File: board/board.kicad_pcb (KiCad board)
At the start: 2 copper layers, 21 x 61 mm, 16 parts, among them J1 002_SPI_2x5, J3 007_ADC_2x5, J4 007_ADC_2x5, J5 007_ADC_2x5, J6 007_ADC_2x5, U1 ADS131M08, Y1 8MhZ

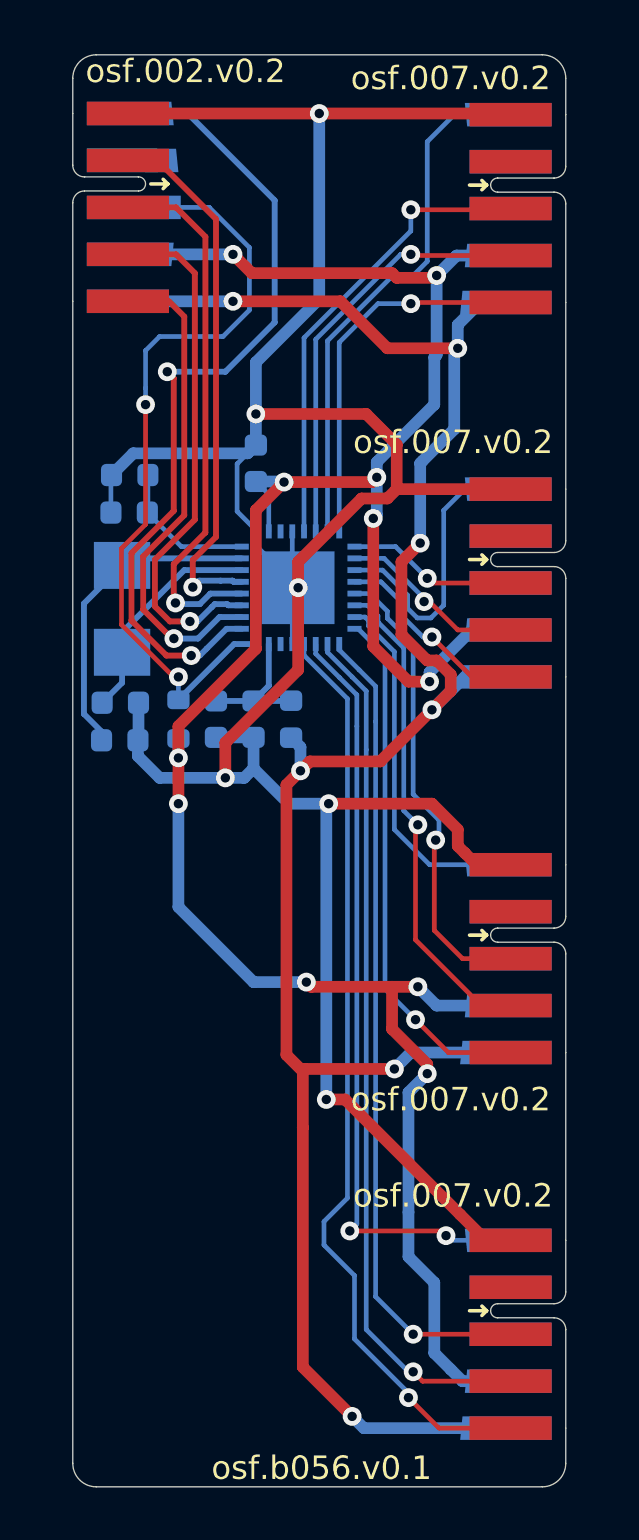
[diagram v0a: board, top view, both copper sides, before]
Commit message: separated gnd and agnd
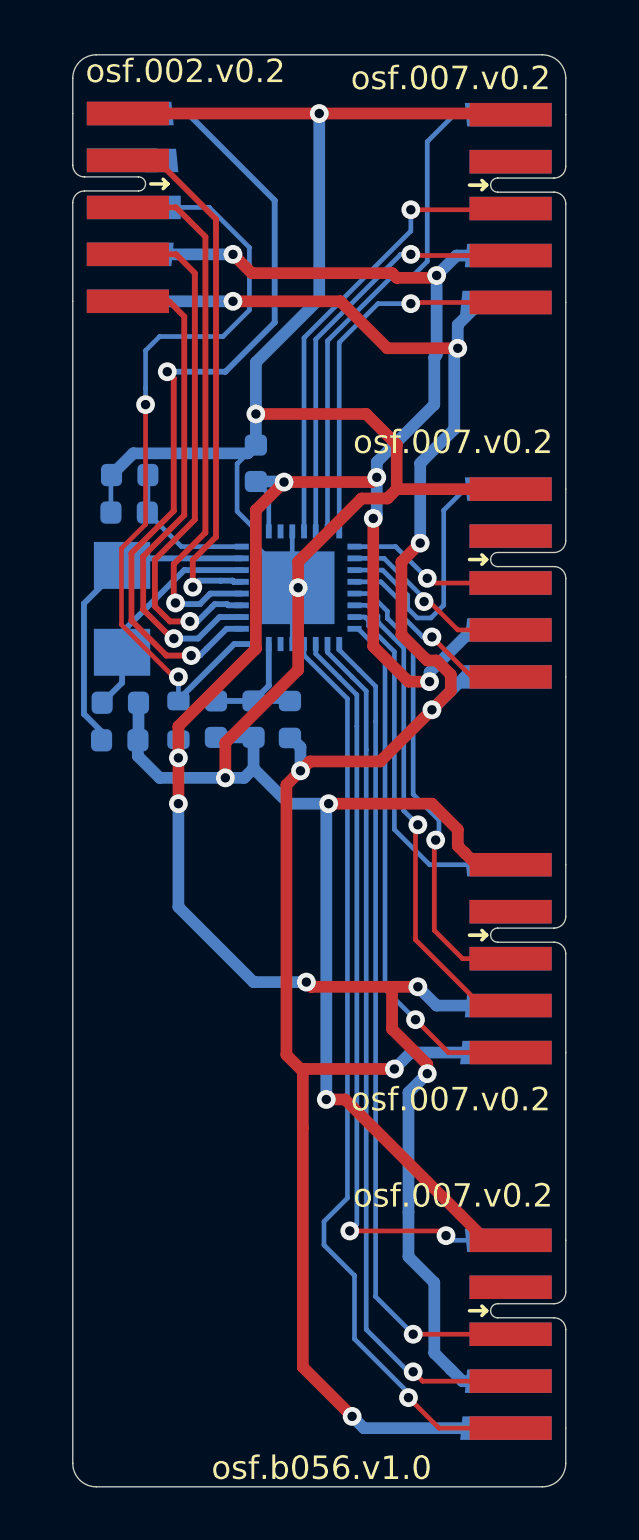
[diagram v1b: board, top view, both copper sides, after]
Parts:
- moved FB1 0.05 mm to (94.2, 73.3)
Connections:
- net /adc/SDI renamed /adc/MOSI
- net /adc/SDO renamed /adc/MISO
- net Net-(C2-Pad1) renamed /adc/AVDD
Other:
- board text added: "osf.b056.v1.0"
- board text removed: "osf.b056.v0.1"

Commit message: Changed adc footprint
ADC footprint was qfn 5x5 but the package is qfn 4x4.
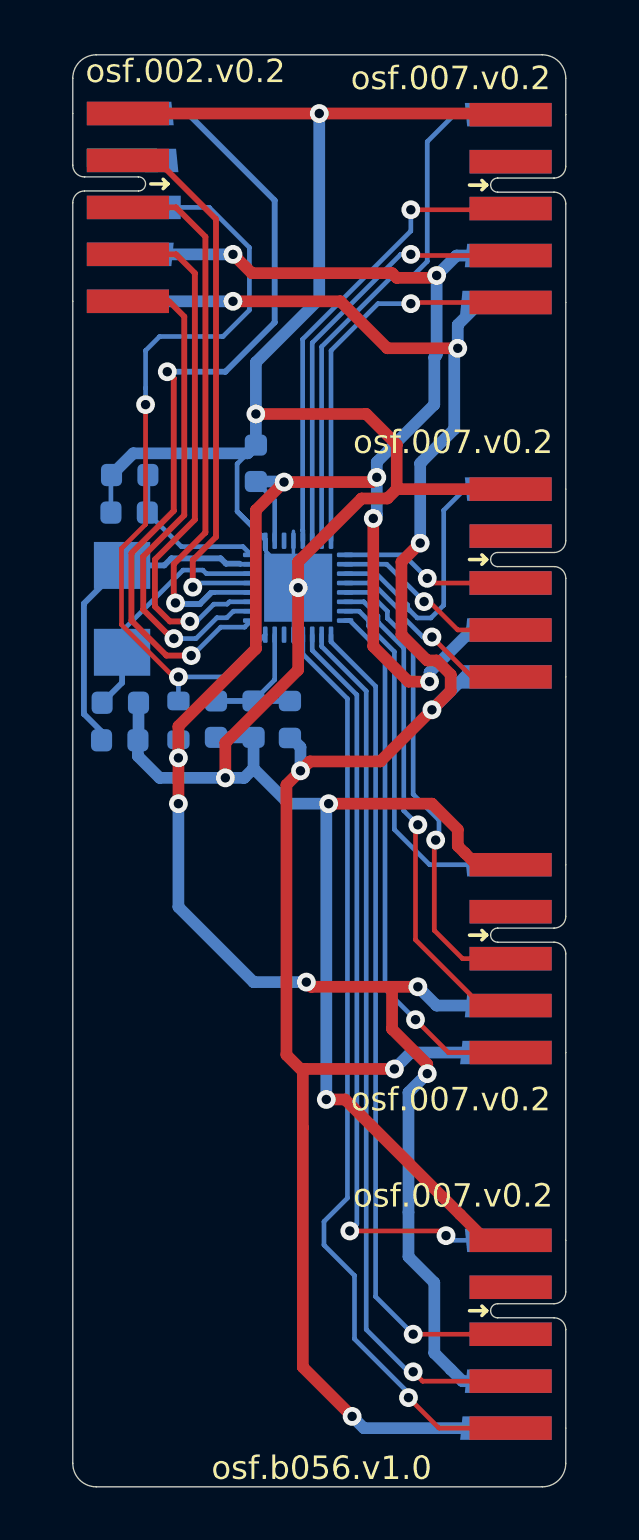
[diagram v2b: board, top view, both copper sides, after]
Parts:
- U1: footprint Package_DFN_QFN:WQFN-32-1EP_5x5mm_P0.5mm_EP3.1x3.1mm -> Package_DFN_QFN:QFN-32-1EP_4x4mm_P0.4mm_EP2.9x2.9mm
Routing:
- net /adc/MISO: track 21.8 -> 24.1 mm
- net GND: track 128.3 -> 130.3 mm
- net Net-(C1-Pad2): track 9.55 -> 10.9 mm
- net /adc/~{CS}: track 35.6 -> 36.2 mm
- net /adc/AIN_5P: track 22.4 -> 23.0 mm
- net /adc/AIN_1P: track 16.1 -> 16.6 mm
- net Net-(C6-Pad1): track 6.24 -> 6.78 mm
- net /adc/AIN_6P: track 33.6 -> 34.1 mm
- net /adc/AIN_1N: track 22.8 -> 23.3 mm
- net /adc/AIN_5N: track 15.5 -> 16.0 mm
- net Net-(C3-Pad1): track 13.7 -> 14.2 mm
- net /adc/~{DRDY}: track 21.0 -> 21.5 mm
- net /adc/AIN_6N: track 36.9 -> 37.4 mm
- net +3.3V: track 106.4 -> 106.9 mm
- net /adc/AVDD: track 5.88 -> 6.39 mm
